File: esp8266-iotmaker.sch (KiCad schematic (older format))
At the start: 49 parts, among them J1 CONN_01X10, J2 CONN_01X10, Q1 S8050, Q2 S8050, SW1 SW_Push, SW2 SW_Push, U1 usb_mini_b, U2 chip-esp8266, U3 CP2102, U4 25Q32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

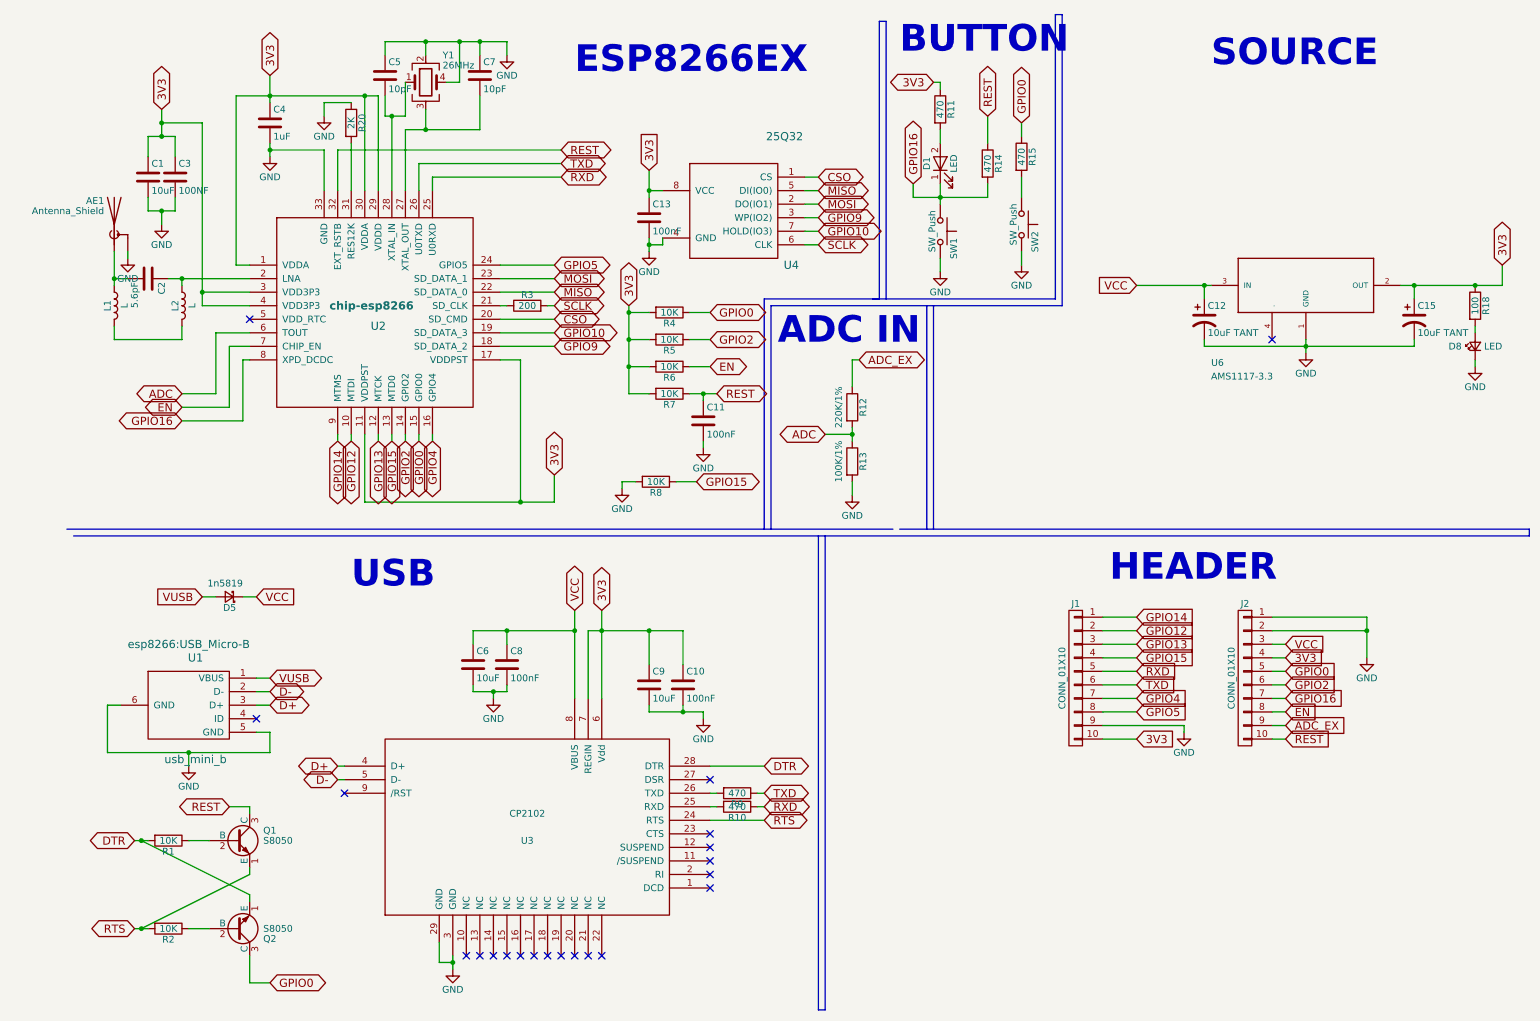
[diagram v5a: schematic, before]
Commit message: add 3d and edit pcb
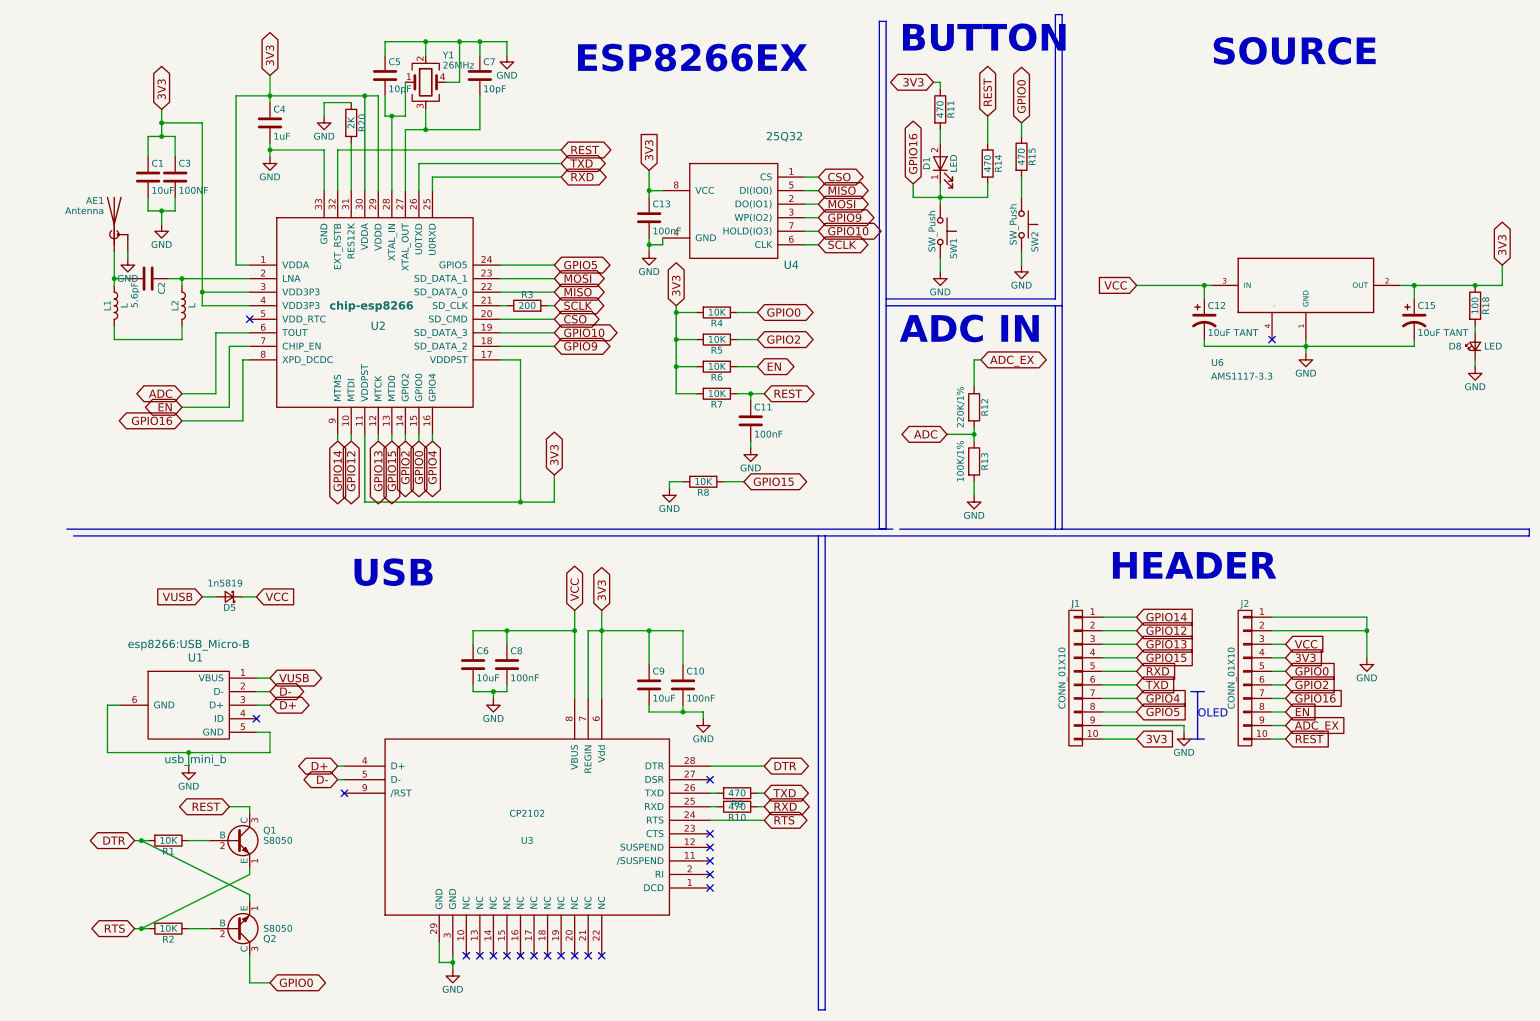
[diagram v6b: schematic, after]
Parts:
- AE1: value Antenna_Shield -> Antenna
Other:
- note added: "OLED\n"
- moved on the sheet: C11, R12, R13, R4, R5, R6, R7, R8

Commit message: edit solder mark
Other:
- moved on the sheet: C12, C15, D1, D8, R11, R12, R13, R14, R15, R18, SW1, SW2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

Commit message: edit readme
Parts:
- Y1: footprint Crystals:Crystal_SMD_2016-4pin_2.0x1.6mm -> Crystals:Crystal_SMD_5032-4pin_5.0x3.2mm
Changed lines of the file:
@@
 F 0 "Y1" H 3225 1150 50  0000 L CNN
 F 1 "26MHz" H 3225 1075 50  0000 L CNN
-F 2 "Crystals:Crystal_SMD_2016-4pin_2.0x1.6mm" H 3100 950 50  0001 C CNN
+F 2 "Crystals:Crystal_SMD_5032-4pin_5.0x3.2mm" H 3100 950 50  0001 C CNN
 F 3 "" H 3100 950 50  0001 C CNN
 	1    3100 950
